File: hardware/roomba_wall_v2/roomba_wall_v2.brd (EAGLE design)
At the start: 39 x 50.8 mm, 13 parts, among them IC1 ATTINY85-20PU, T1 2N2222

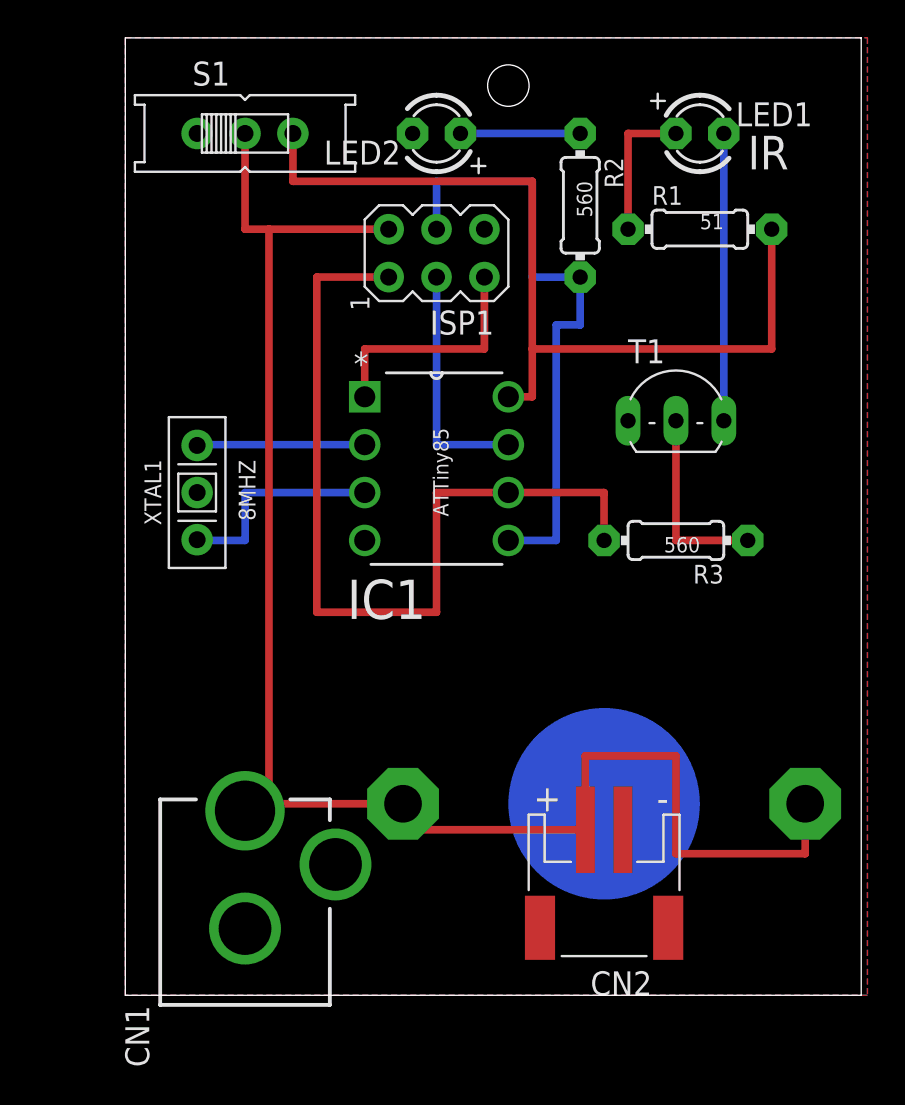
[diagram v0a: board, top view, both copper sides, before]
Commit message: PCB layout, rev B 1/3 smaller, with mounting holes and cutout for the battery holder
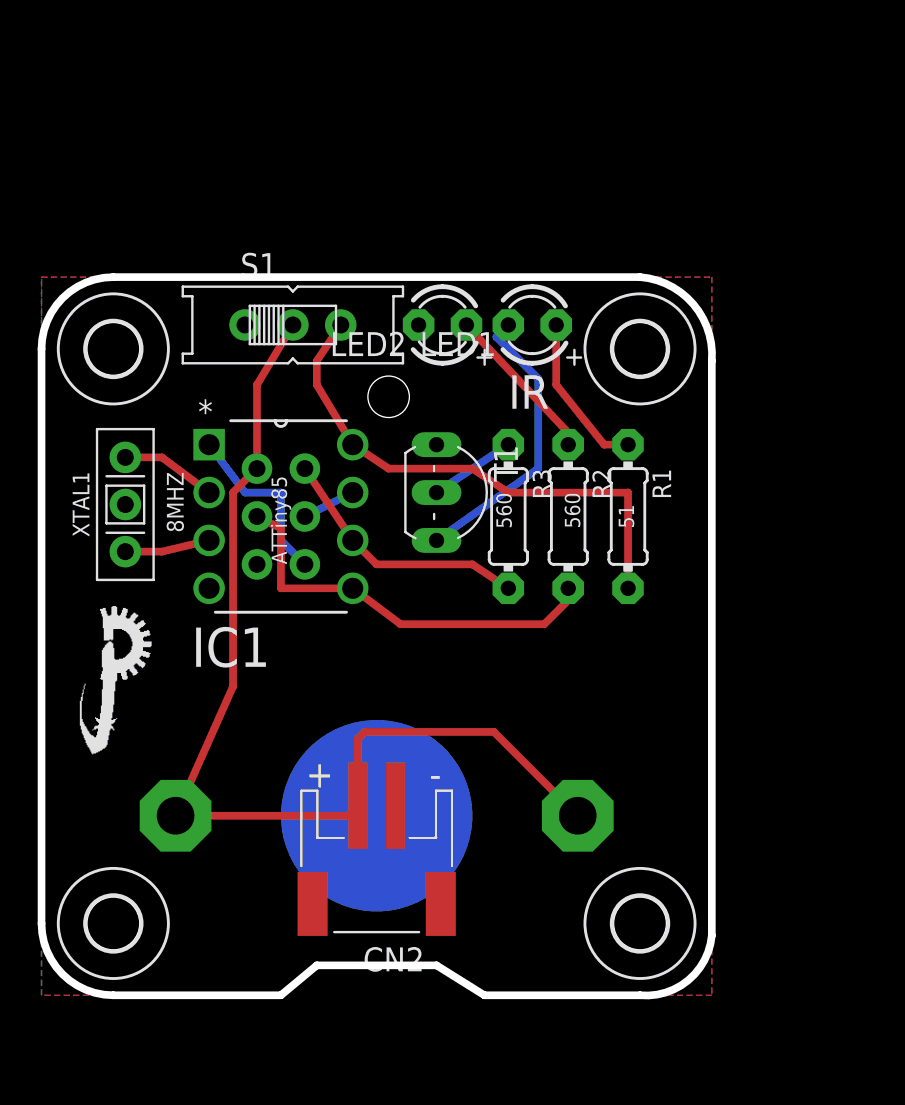
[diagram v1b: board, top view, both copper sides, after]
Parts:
- removed CN1: (no value), adafruit:DCJACK_2MM_PTH
- added H1, H2, H3, H4: MOUNT-HOLE2.8, holes:2,8
- added U$2, U$3: (no value), petezah:LOGO_TINY
- moved R2 16.5 mm to (23.5, 25.4)
- moved ISP1 16.2 mm to (8.26, 25.4), flipped to the bottom, turned to 0 degrees
- moved R1 15.7 mm to (26.7, 25.4), turned to 270 degrees
- moved LED1 13.5 mm to (21.6, 35.6), turned to 180 degrees
- moved T1 12.5 mm to (17.8, 26.7), turned to 270 degrees
- moved CN2 12.1 mm to (13.3, 6.35)
- moved U$1 12.1 mm to (13.3, 9.53)
- moved S1 10.5 mm to (8.89, 35.6)
- moved LED2 10.2 mm to (16.8, 35.6)
- moved R3 8.98 mm to (20.3, 25.4), turned to 270 degrees
- moved IC1 8.64 mm to (12.1, 21.6)
- moved XTAL1 3.86 mm to (0.00, 26.0)
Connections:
- net +3V3: no longer CN1.PWR
- net GND: no longer CN1.GND, CN1.GNDBREAK
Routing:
- net MISO: track 45.7 -> 13.7 mm
- net +3V3: track 86.4 -> 54.8 mm
- net VCC: track 47.0 -> 27.7 mm
- net MOSI: track 33.0 -> 21.6 mm
- net SCK: track 12.7 -> 2.84 mm
- net N$2: track 11.5 -> 4.51 mm
- net N$5: track 10.2 -> 4.58 mm
- net N$1: track 8.93 -> 5.06 mm
- net RST: track 12.7 -> 9.42 mm
- net N$6: track 6.35 -> 8.50 mm
- net N$3: track 7.62 -> 8.51 mm
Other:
- board size 39 x 50.8 mm -> 35.6 x 38.1 mm
- board text added: "Roomba Virtual Wall v2 Board revision B"
- board text removed: "Roomba Virtual Wall v2 Board revision A"
